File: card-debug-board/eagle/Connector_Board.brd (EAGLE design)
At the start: 69.9 x 34.3 mm, 32 parts, among them J1 ORESAT-DEBUG-CONNECTOR-CARD, J3 USB_A_SMT_FEMALE, Q1 MOSFET-PCH-SOT23-6, U1 FT230XS-R

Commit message: Design review changes made
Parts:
- moved JP1 4.80 mm to (22.2, 14.6), turned to 0 degrees
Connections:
- net N$1 renamed VBUS_UART
- net SLAVE_D_N renamed USB-DEVICE_D_N
- net SLAVE_D_P renamed USB-DEVICE_D_P
- new net VCCIO: C6.1, R3.2, R4.2, R5.2, R6.2, R7.2, R8.2, U1.10, U1.11, U1.3
- net VSER: now also C7.1, C8.1, Q1.1, Q1.2, Q1.5, Q1.6; no longer C6.1, R3.2, R4.2, R5.2, R6.2, R7.2, R8.2, U1.10, U1.11, U1.3
- net VUSB: no longer C7.1, C8.1, Q1.1, Q1.2, Q1.5, Q1.6
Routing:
- net VUSB: track 8.72 -> 9.81 mm
- net VBUS_OUT: track 8.71 -> 7.67 mm
- net USB-DEVICE_D_P: track 25.3 -> 26.2 mm
- added copper zone on layer 1, net VCCIO
- removed copper zone on layer 1, net VUSB

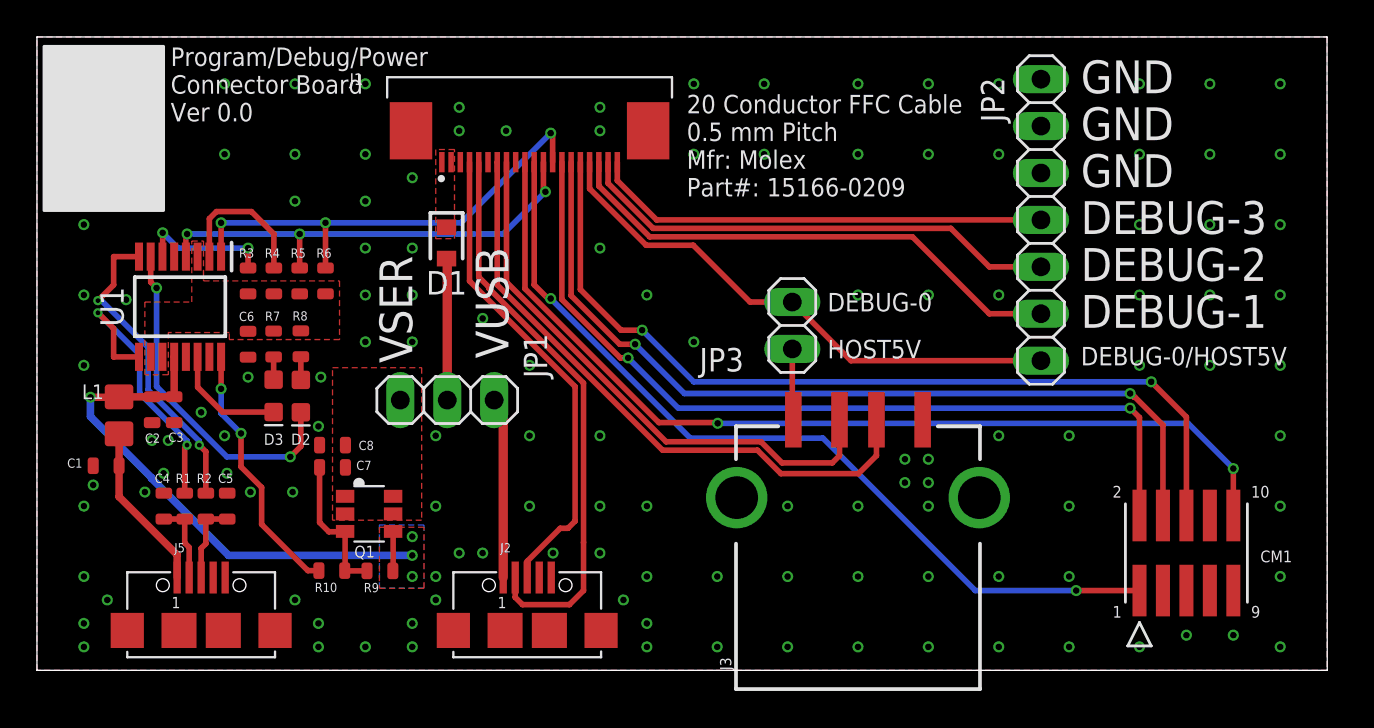
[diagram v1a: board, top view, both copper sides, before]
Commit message: Made changes per design review
Added test points for RX TX rewire, made board smaller
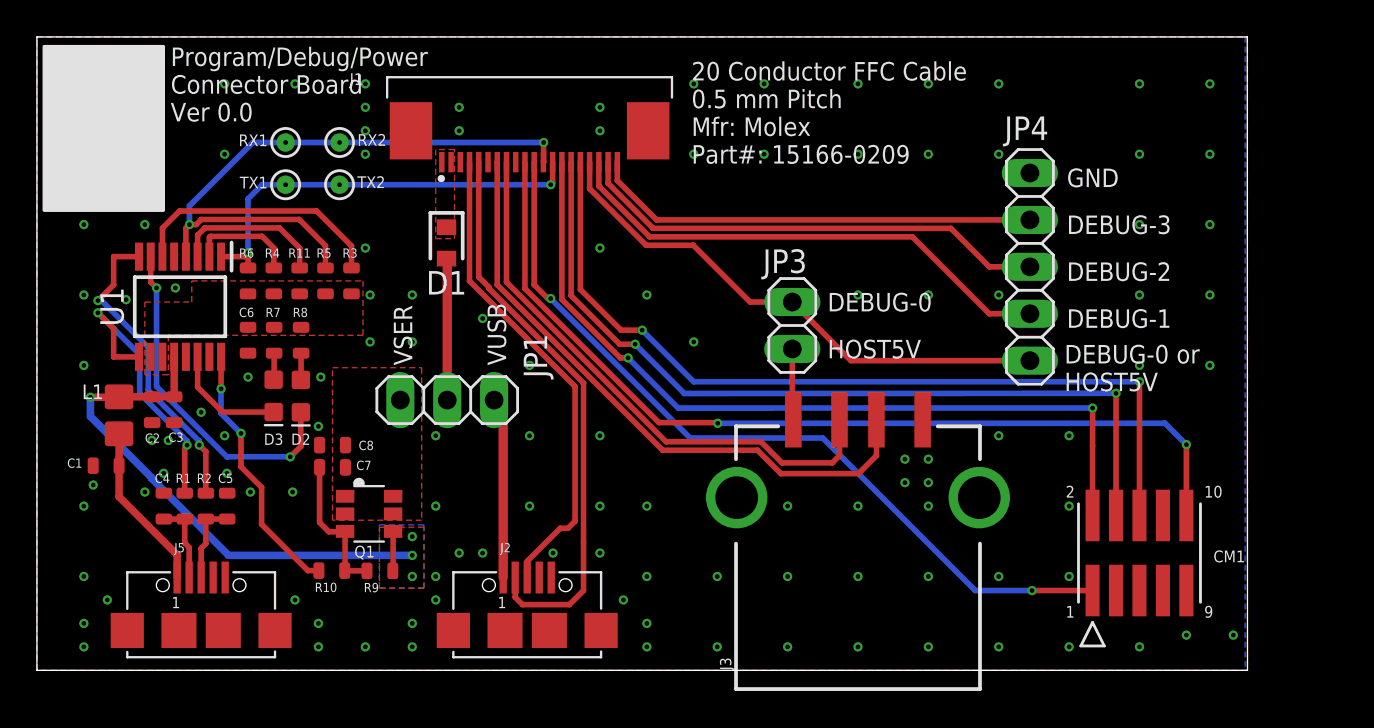
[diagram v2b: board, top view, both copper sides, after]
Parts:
- removed JP2: (no value), pinhead:1X07
- added JP4: (no value), pinhead:1X05
- added R11: 10k, oresat-rcl:.0603-C-NOSILK
- added RX1, RX2, TX1, TX2: TP1MM-TP, oresat-misc:1MM-TP
- moved R3 5.60 mm to (17.0, 21.1)
- moved R6 4.19 mm to (11.4, 21.1)
- moved CM1 2.54 mm to (59.7, 6.35)
- moved R5 1.40 mm to (15.6, 21.1)
- moved C6 0.22 mm to (11.4, 17.9)
- moved R7 0.20 mm to (12.8, 17.9)
- moved R8 0.19 mm to (14.3, 17.9)
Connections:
- new net VCCIO_P: C6.1, R11.2, R3.2, R4.2, R5.2, R6.2, R7.2, R8.2, U1.10, U1.11
- net DEBUG-0/HOST5V: now also JP4.1; no longer JP2.1
- net DEBUG-1: now also JP4.2; no longer JP2.2
- net DEBUG-2: now also JP4.3; no longer JP2.3
- net DEBUG-3: now also JP4.4; no longer JP2.4
- net GND: now also JP4.5; no longer JP2.5, JP2.6, JP2.7
- net RXD: now also RX1.TP, RX2.TP
- net TXD: now also TX1.TP, TX2.TP
- net VCCIO: now also R11.1; no longer C6.1, R3.2, R4.2, R5.2, R6.2, R7.2, R8.2, U1.10, U1.11
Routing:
- net RXD: track 25.1 -> 33.8 mm, vias 3 -> 2
- net VCCIO: track 0.00 -> 8.38 mm
- net CTS#: track 7.34 -> 14.1 mm, vias 2 -> 0
- net VTARGET: track 46.3 -> 43.7 mm
- net TXD: track 25.8 -> 23.3 mm, vias 3 -> 2
- net SWDIO: track 46.7 -> 44.4 mm
- net RTS#: track 8.05 -> 5.89 mm
- net NRST: track 51.8 -> 50.0 mm
- net SWCLK: track 47.1 -> 45.5 mm
- net SWO: track 47.9 -> 46.5 mm
- net DEBUG-3: track 24.8 -> 24.2 mm
- net DEBUG-2: track 26.5 -> 25.9 mm
- net DEBUG-1: track 28.1 -> 27.5 mm
- net DEBUG-0/HOST5V: track 29.7 -> 29.1 mm
- added copper zone on layer 1, net VCCIO_P
- removed copper zone on layer 1, net VCCIO
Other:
- board size 69.9 x 34.3 mm -> 65.5 x 34.3 mm
- board text added: "DEBUG-0 or HOST5V"
- board text removed: "DEBUG-0/HOST5V"

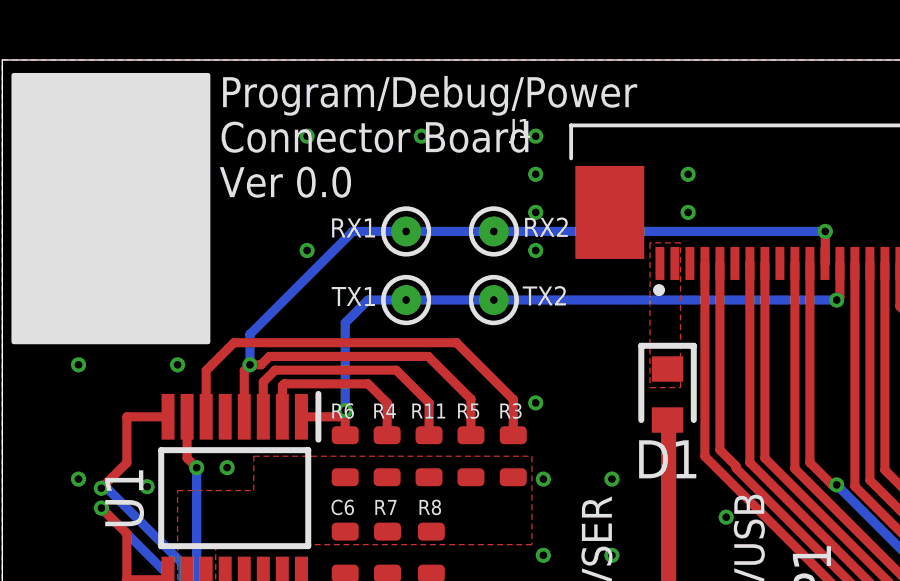
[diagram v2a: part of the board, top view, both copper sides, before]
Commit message: Added masking for TX and RX
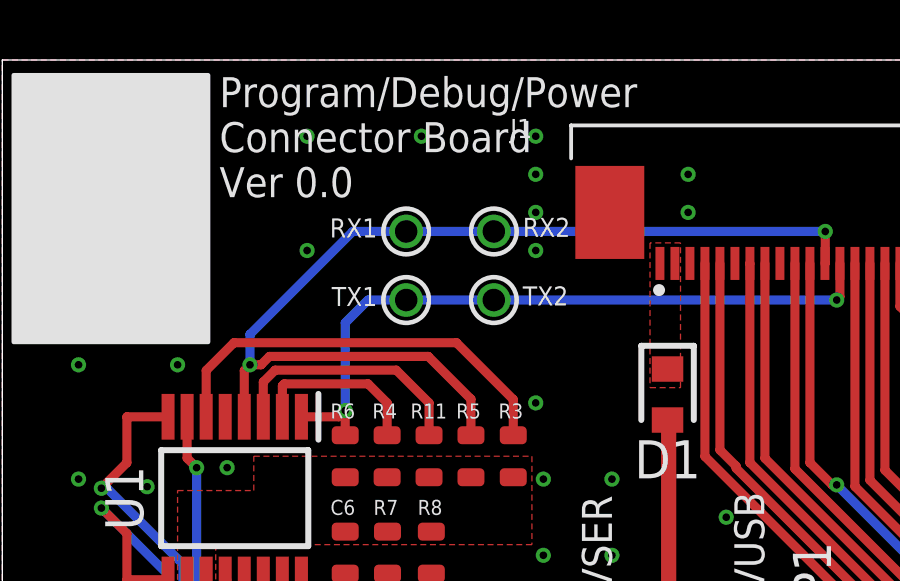
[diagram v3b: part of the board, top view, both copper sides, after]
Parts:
- RX1, RX2, TX1, TX2: value TP1MM-TP -> (none); device oresat-misc:1MM-TP -> oresat-misc:TP
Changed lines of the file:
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@@
 <setting verticaltext="up"/>
 </settings>
-<grid distance="0.127" unitdist="mm" unit="mm" style="lines" multiple="1" display="yes" altdistance="0.0127" altunitdist="mm" altunit="mm"/>
+<grid distance="0.1" unitdist="mm" unit="mm" style="lines" multiple="1" display="yes" altdistance="0.001" altunitdist="mm" altunit="mm"/>
 <layers>
 <layer number="1" name="Top" color="4" fill="1" visible="yes" active="yes"/>
@@
 Connector Board
 Ver 0.0</text>
+<polygon width="0.127" layer="30">
+<vertex x="14.2" y="29.7"/>
+<vertex x="15.6" y="29.7"/>
+<vertex x="15.6" y="25.3"/>
+<vertex x="14.2" y="25.3"/>
+</polygon>
 </plain>
 <attributes>
@@
 <attribute name="VALUE" x="12.674" y="22.082" size="0.8" layer="27" font="vector" ratio="15" rot="R270"/>
 </element>
-<element name="RX1" library="oresat-misc" package="1MM-TP" package3d_urn="urn:adsk.eagle:package:27946/1" value="TP1MM-TP" x="13.462" y="28.575" smashed="yes">
+<element name="RX1" library="oresat-misc" package="TP" package3d_urn="urn:adsk.eagle:package:27946/1" value="" x="13.462" y="28.575" smashed="yes">
 <attribute name="NAME" x="12.496" y="29.01" size="0.635" layer="25" font="vector" ratio="20" rot="R180"/>
 <attribute name="POPULARITY" value="12" x="13.462" y="28.575" size="1" layer="27" display="off"/>
-<attribute name="TP_SIGNAL_NAME" value="" x="13.462" y="28.575" size="1" layer="27" display="off"/>
-<attribute name="VALUE" x="13.462" y="28.575" size="0.0254" layer="27"/>
-</element>
-<element name="RX2" library="oresat-misc" package="1MM-TP" package3d_urn="urn:adsk.eagle:package:27946/1" value="TP1MM-TP" x="16.383" y="28.575" smashed="yes">
+<attribute name="VALUE" value="" x="13.462" y="28.575" size="0.0254" layer="27"/>
+</element>
+<element name="RX2" library="oresat-misc" package="TP" package3d_urn="urn:adsk.eagle:package:27946/1" value="" x="16.383" y="28.575" smashed="yes">
 <attribute name="NAME" x="17.349" y="28.394" size="0.635" layer="25" font="vector" ratio="20"/>
 <attribute name="POPULARITY" value="12" x="16.383" y="28.575" size="1" layer="27" display="off"/>
-<attribute name="TP_SIGNAL_NAME" value="" x="16.383" y="28.575" size="1" layer="27" display="off"/>
-<attribute name="VALUE" x="16.383" y="28.575" size="0.0254" layer="27"/>
-</element>
-<element name="TX1" library="oresat-misc" package="1MM-TP" package3d_urn="urn:adsk.eagle:package:27946/1" value="TP1MM-TP" x="13.462" y="26.289" smashed="yes">
+<attribute name="VALUE" value="" x="16.383" y="28.575" size="0.0254" layer="27"/>
+</element>
+<element name="TX1" library="oresat-misc" package="TP" package3d_urn="urn:adsk.eagle:package:27946/1" value="" x="13.462" y="26.289" smashed="yes">
 <attribute name="NAME" x="12.496" y="26.724" size="0.635" layer="25" font="vector" ratio="20" rot="R180"/>
 <attribute name="POPULARITY" value="12" x="13.462" y="26.289" size="1" layer="27" display="off"/>
-<attribute name="TP_SIGNAL_NAME" value="" x="13.462" y="26.289" size="1" layer="27" display="off"/>
-<attribute name="VALUE" x="13.462" y="26.289" size="0.0254" layer="27"/>
-</element>
-<element name="TX2" library="oresat-misc" package="1MM-TP" package3d_urn="urn:adsk.eagle:package:27946/1" value="TP1MM-TP" x="16.383" y="26.289" smashed="yes">
+<attribute name="VALUE" value="" x="13.462" y="26.289" size="0.0254" layer="27"/>
+</element>
+<element name="TX2" library="oresat-misc" package="TP" package3d_urn="urn:adsk.eagle:package:27946/1" value="" x="16.383" y="26.289" smashed="yes">
 <attribute name="NAME" x="17.349" y="26.108" size="0.635" layer="25" font="vector" ratio="20"/>
 <attribute name="POPULARITY" value="12" x="16.383" y="26.289" size="1" layer="27" display="off"/>
-<attribute name="TP_SIGNAL_NAME" value="" x="16.383" y="26.289" size="1" layer="27" display="off"/>
-<attribute name="VALUE" x="16.383" y="26.289" size="0.0254" layer="27"/>
+<attribute name="VALUE" value="" x="16.383" y="26.289" size="0.0254" layer="27"/>
 </element>
 </elements>

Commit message: Changed from VBUSP to VBUS for power out
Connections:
- net VBUSP renamed VBUS
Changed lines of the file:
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@@
 <drawing>
 <settings>
-<setting alwaysvectorfont="yes"/>
+<setting alwaysvectorfont="no"/>
 <setting verticaltext="up"/>
 </settings>
@@
 <wire x1="9.0932" y1="23.9522" x2="13.1318" y2="23.9522" width="0.3048" layer="1"/>
 </signal>
-<signal name="VBUSP">
+<signal name="VBUS">
 <contactref element="D1" pad="1"/>
 <contactref element="J1" pad="1"/>

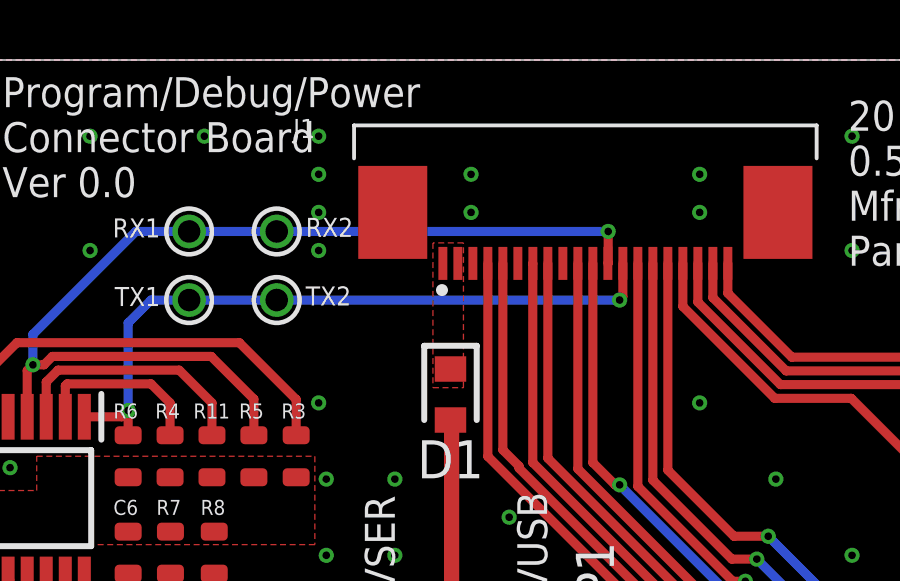
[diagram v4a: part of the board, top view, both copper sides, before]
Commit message: Swapped TX RX traces
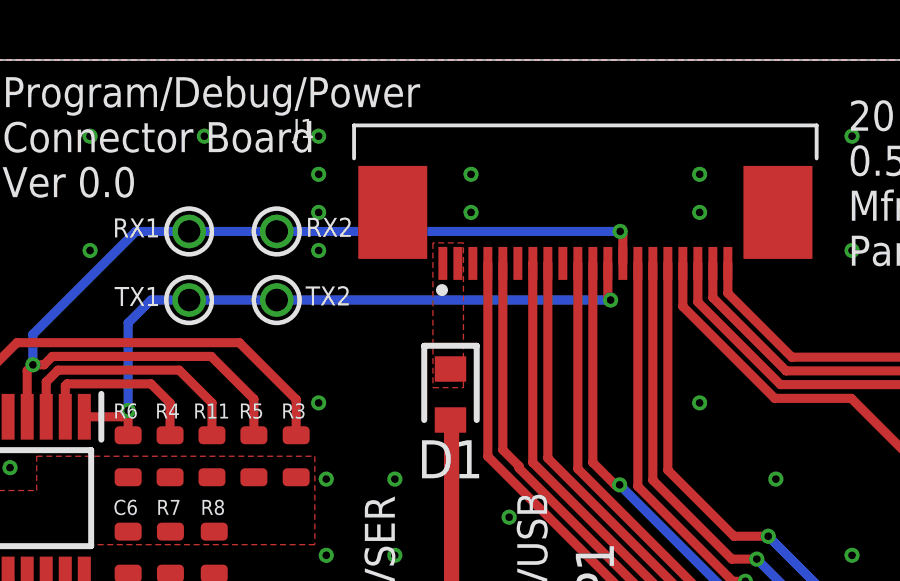
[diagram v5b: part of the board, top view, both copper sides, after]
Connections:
- net RXD: now also J1.13; no longer J1.12
- net TXD: now also J1.12; no longer J1.13
